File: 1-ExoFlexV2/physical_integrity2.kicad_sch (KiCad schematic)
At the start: 30 parts, among them J82 100k, J83 100k, J84 100k, J85 100k, J86 100k, J87 100k, U74 SN74LVC1G32DBVR, U75 SN74LVC1G32DBVR, U76 SN74LVC1G32DBVR, U77 SN74LVC1G32DBVR, U79 SN74LVC1G32DBVR

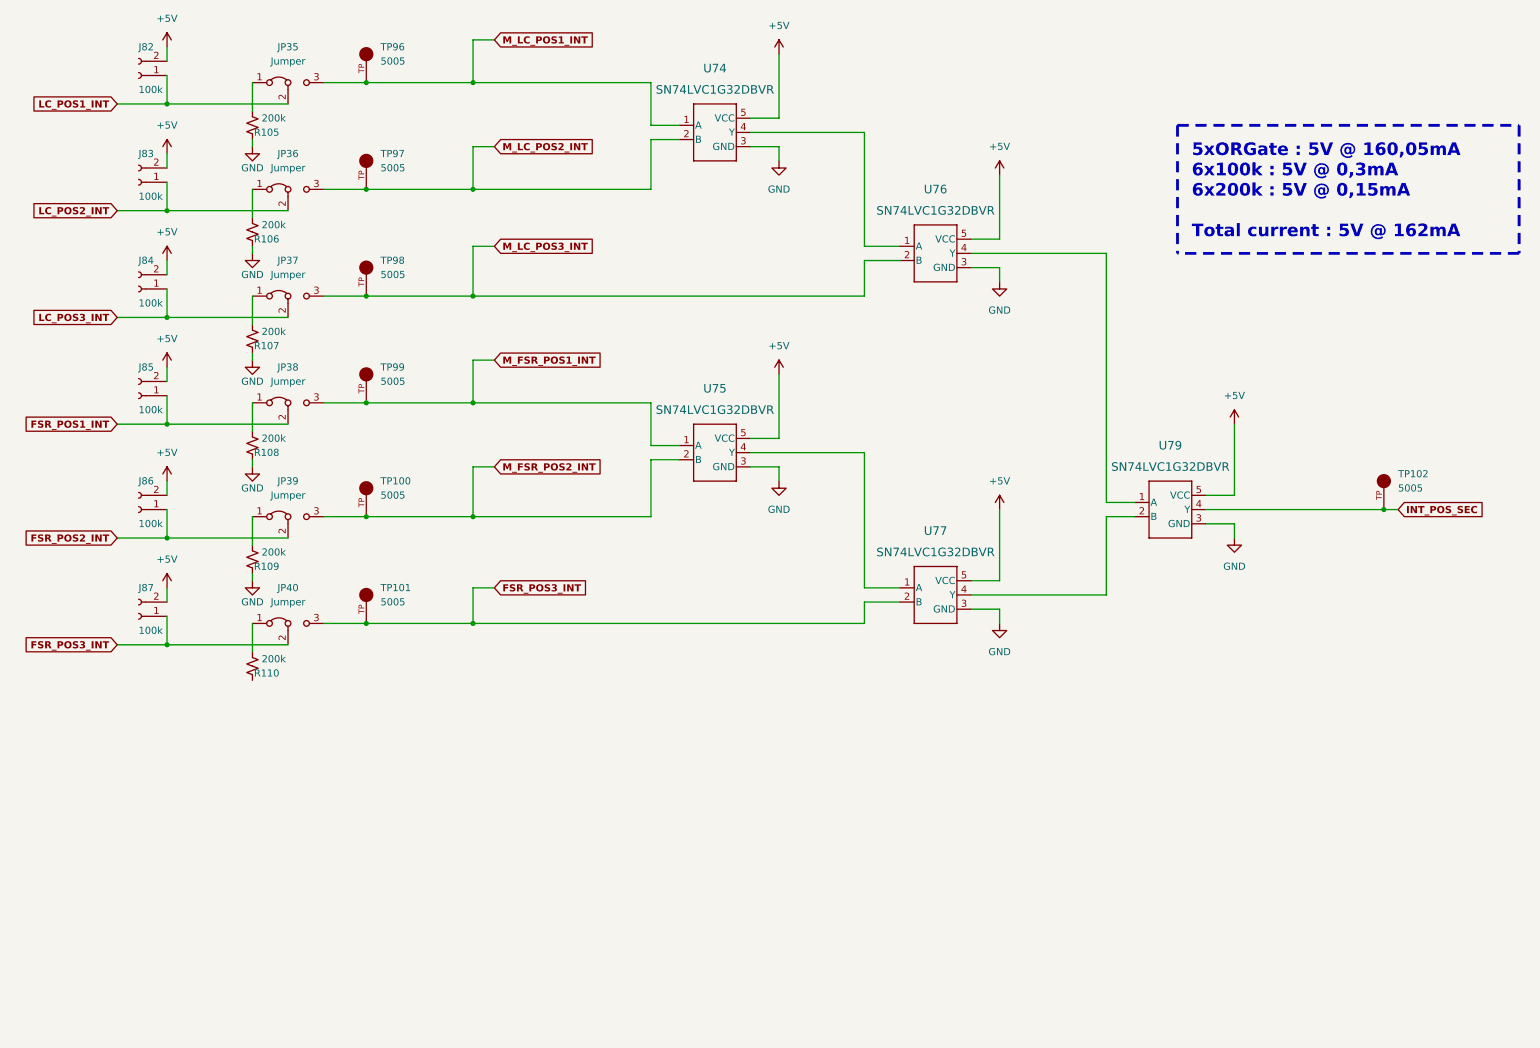
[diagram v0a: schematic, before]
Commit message: Chokes et RC
- Ajout des RF chokes
- Changement des résistance pour 0805
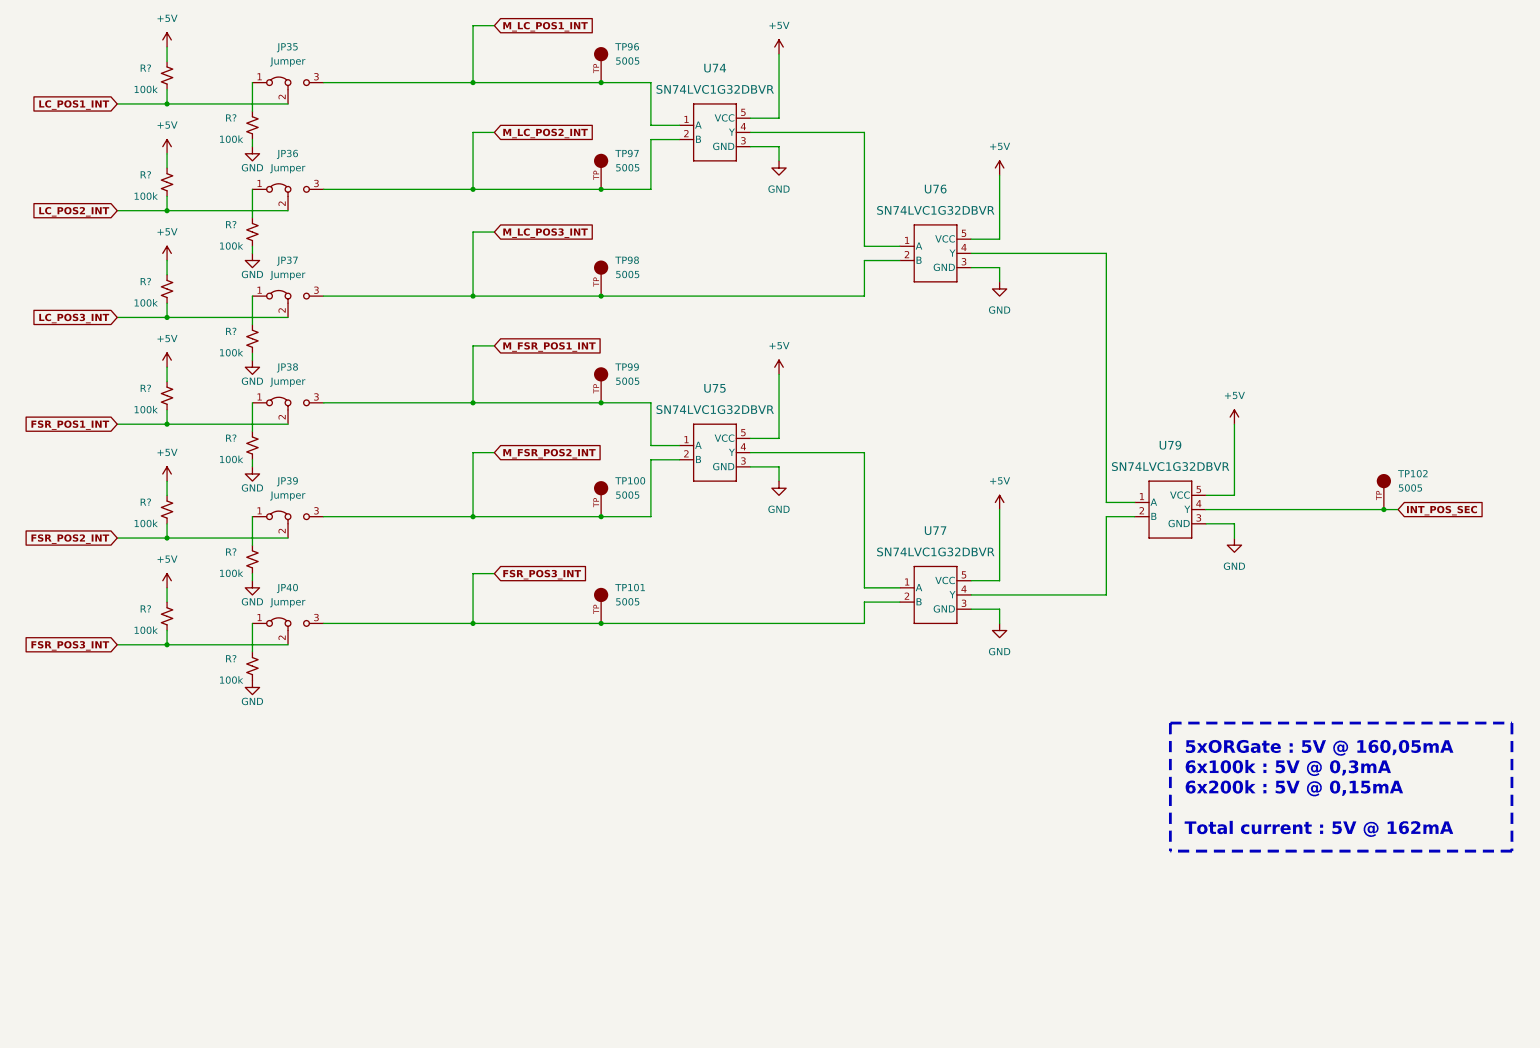
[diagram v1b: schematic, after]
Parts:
- removed J82, J83, J84, J85, J86, J87: 100k, Connector_PinHeader_2.54mm:PinHeader_1x02_P2.54mm_Vertical, symbol Connector:Conn_01x02_Female
- removed R105, R106, R107, R108, R109, R110: 200k, Resistor_SMD:R_0603_1608Metric, symbol Device:R_Small_US
- added R? (x12): 100k, Resistor_SMD:R_0805_2012Metric, symbol Device:R_Small_US
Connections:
- net +5V: now also R?.1, R?.1, R?.1, R?.1, R?.1, R?.1
- net FSR_POS1_INT: now also R?.2
- net FSR_POS2_INT: now also R?.2
- net FSR_POS3_INT: now also R?.2
- net GND: now also R?.2, R?.2, R?.2, R?.2, R?.2, R?.2
- net LC_POS1_INT: now also R?.2
- net LC_POS2_INT: now also R?.2
- net LC_POS3_INT: now also R?.2
- net at JP39.1 (A): now also R?.1
- net at JP38.1 (A): now also R?.1
- net at JP40.1 (A): now also R?.1
- net at JP37.1 (A): now also R?.1
- net at JP36.1 (A): now also R?.1
- net at JP35.1 (A): now also R?.1
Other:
- moved on the sheet: TP100, TP101, TP96, TP97, TP98, TP99

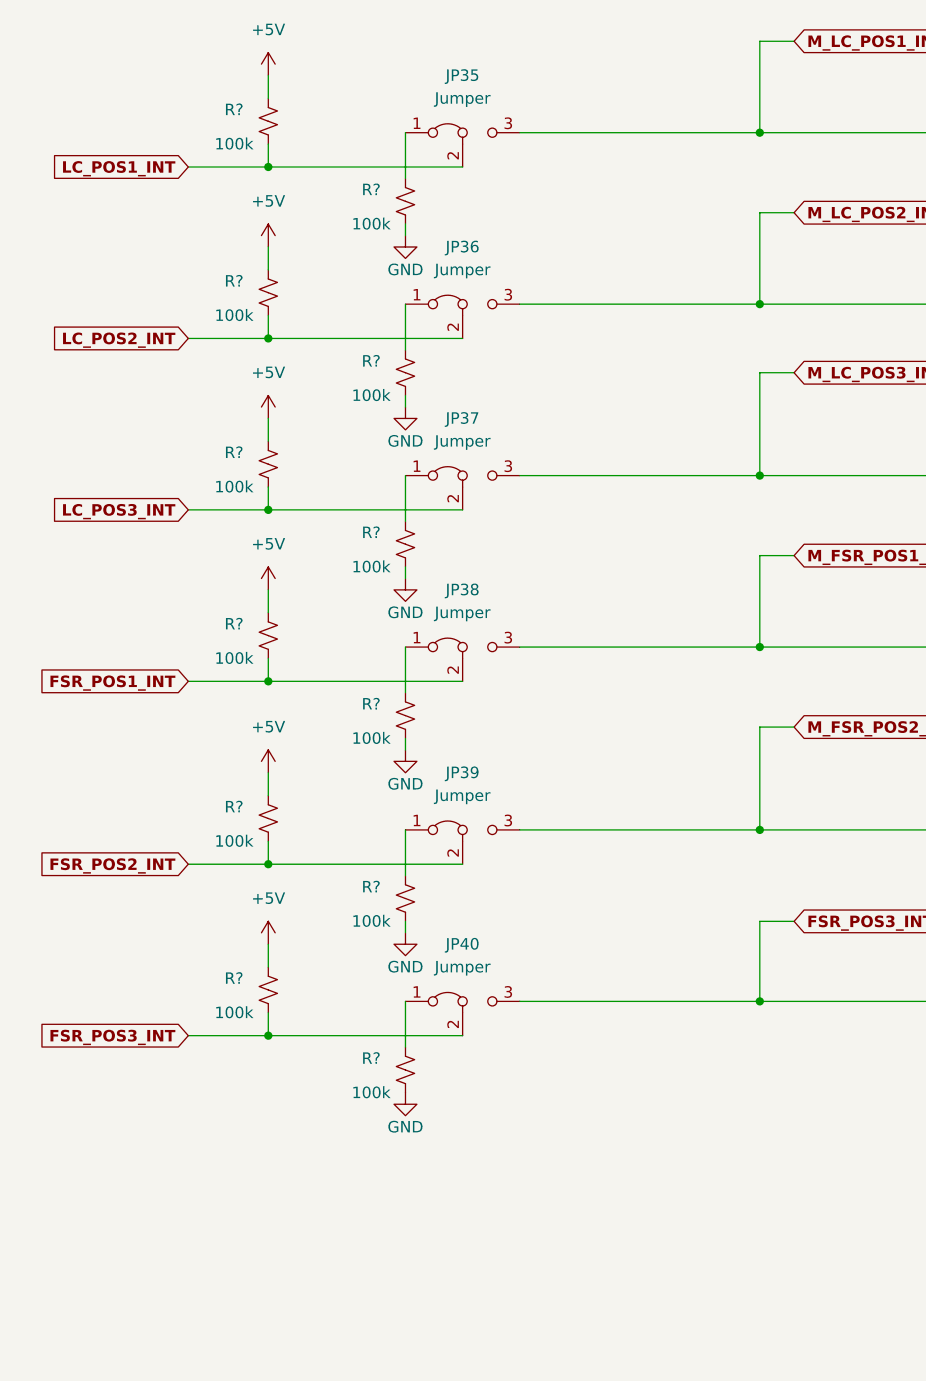
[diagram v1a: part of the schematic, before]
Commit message: Trimmer et jumper
-Changement de symbole de jumper
-Ajout des des trimmer aux endroits nécessaires
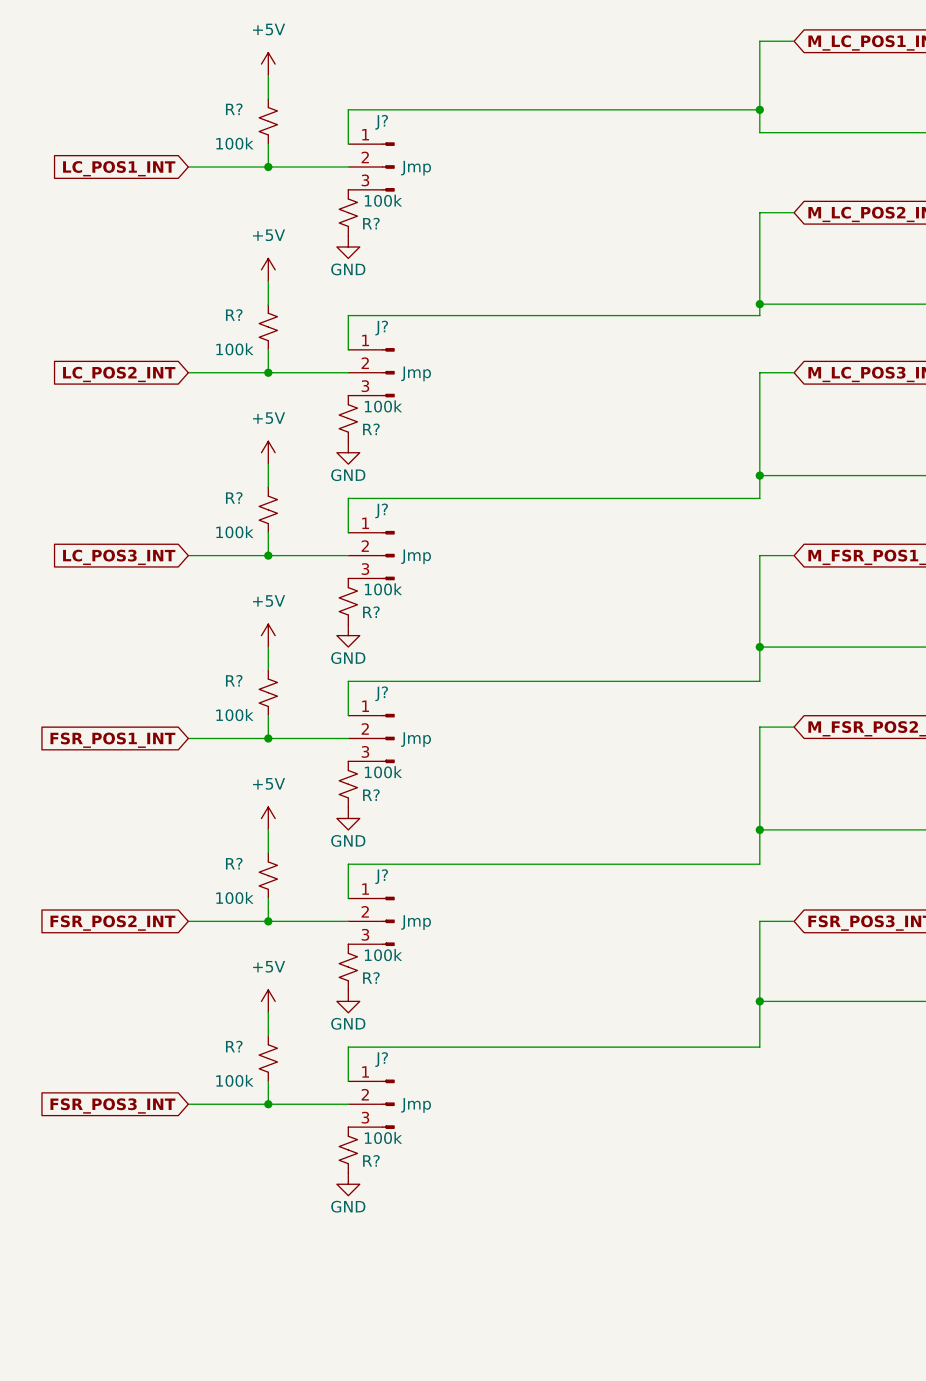
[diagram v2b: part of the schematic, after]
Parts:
- removed JP35, JP36, JP37, JP38, JP39, JP40: Jumper, Connector_PinHeader_2.54mm:PinHeader_1x03_P2.54mm_Vertical, symbol Jumper:Jumper_3_Bridged12
- removed R? (x6): 100k, Resistor_SMD:R_0805_2012Metric, symbol Device:R_Small_US
- added J? (x6): Jmp, symbol Connector:Conn_01x03_Male
- added R? (x6): 100k, Resistor_SMD:R_0805_2012Metric, symbol Device:R_Small_US
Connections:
- net FSR_POS1_INT: now also J?.2 (Pin_2)
- net FSR_POS2_INT: now also J?.2 (Pin_2)
- net FSR_POS3_INT: now also J?.1 (Pin_1), J?.2 (Pin_2)
- net GND: now also R?.2, R?.2, R?.2, R?.2, R?.2, R?.2
- net LC_POS1_INT: now also J?.2 (Pin_2)
- net LC_POS2_INT: now also J?.2 (Pin_2)
- net LC_POS3_INT: now also J?.2 (Pin_2)
- net M_FSR_POS1_INT: now also J?.1 (Pin_1)
- net M_FSR_POS2_INT: now also J?.1 (Pin_1)
- net M_LC_POS1_INT: now also J?.1 (Pin_1)
- net M_LC_POS2_INT: now also J?.1 (Pin_1)
- net M_LC_POS3_INT: now also J?.1 (Pin_1)
- new net: J?.3 (Pin_3), R?.1 (x6)
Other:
- moved on the sheet: R?

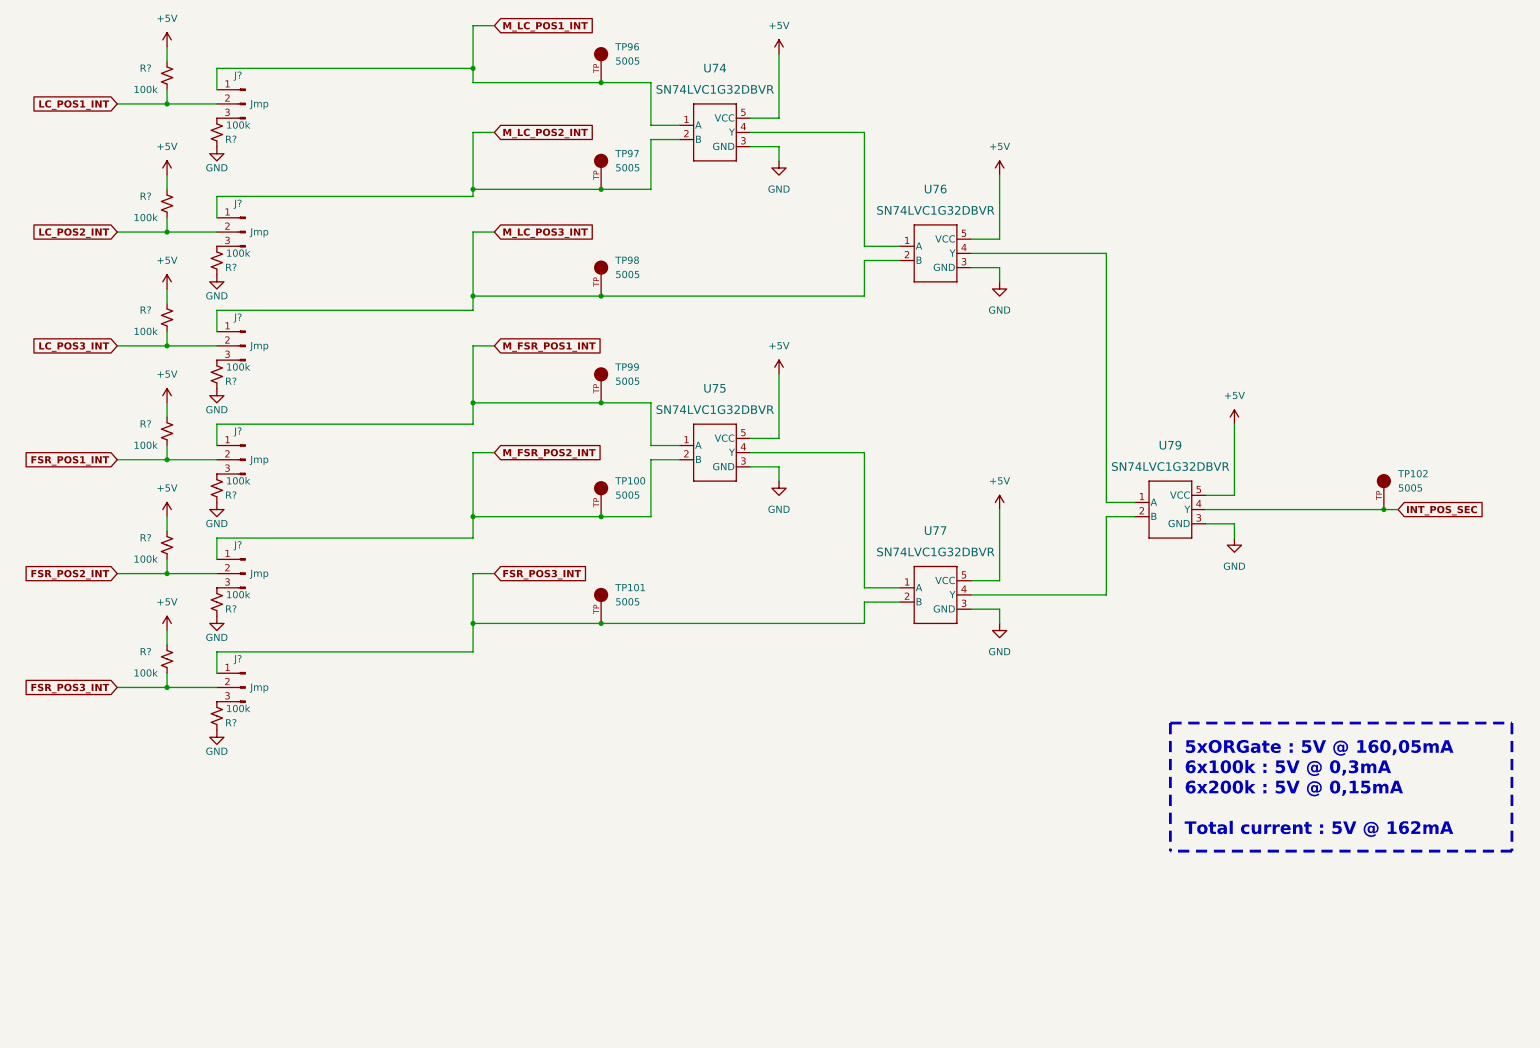
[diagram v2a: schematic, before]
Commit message: Test points et notes
- Ajout de tous les tests point nécessaires
-  Ajoute des sections de notes dans chaque page
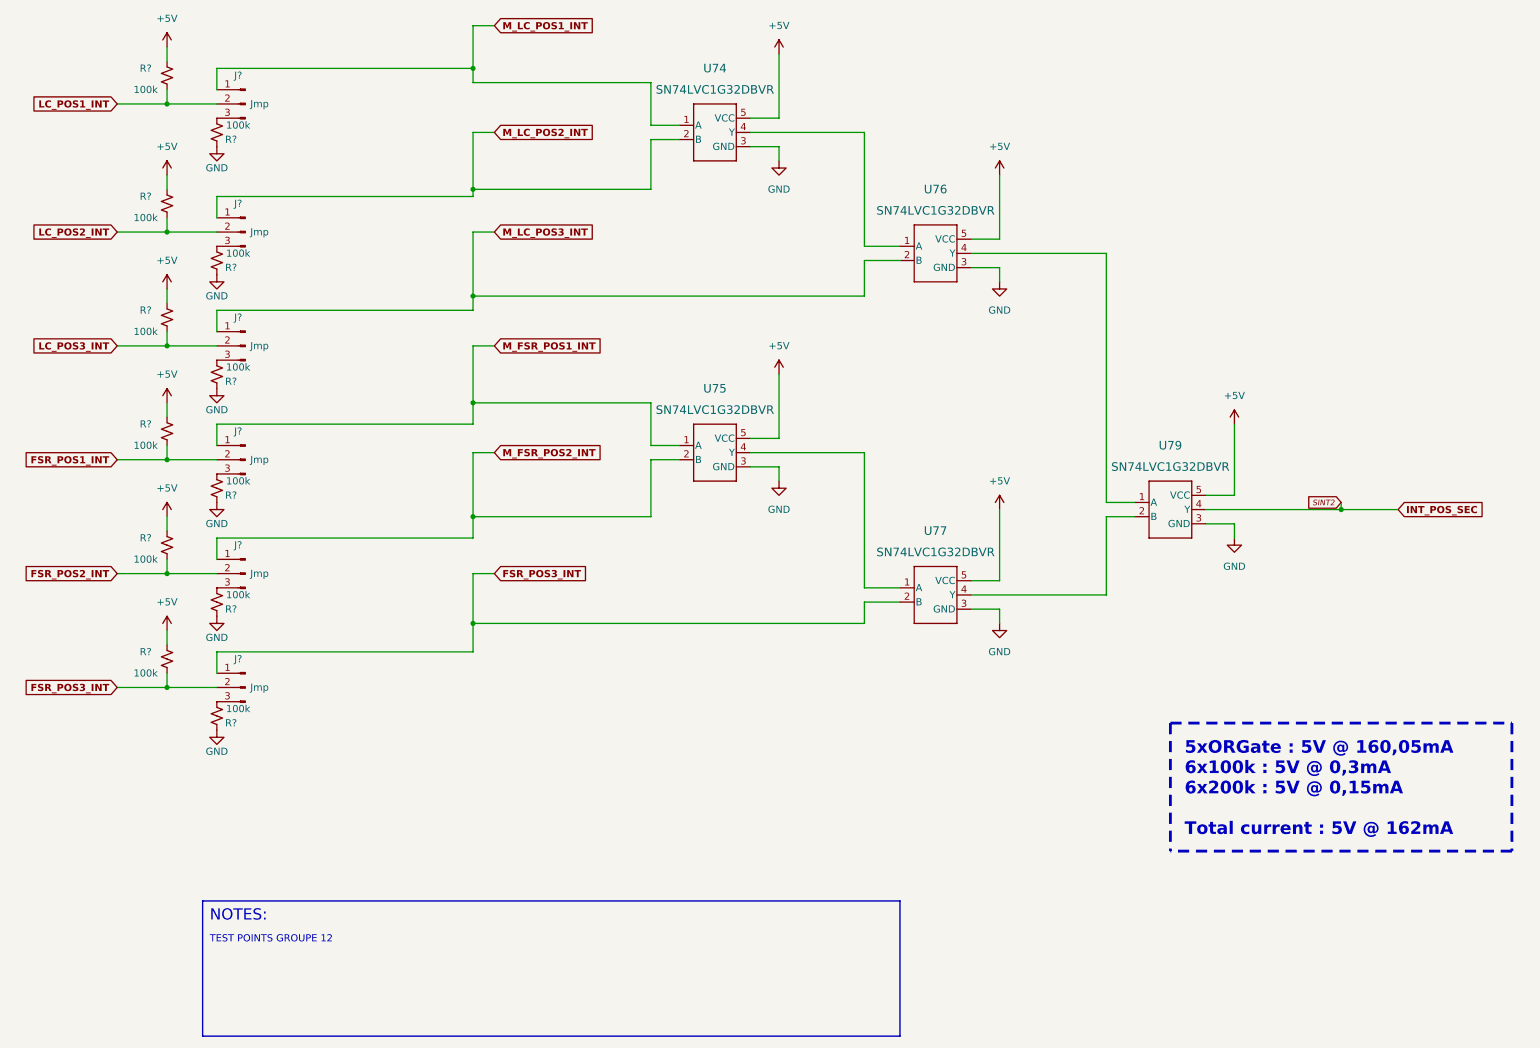
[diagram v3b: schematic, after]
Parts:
- removed TP100, TP101, TP102, TP96, TP97, TP98, TP99: 5005, FootPrint:KEYSTONE_5005, symbol SymLib:5005
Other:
- note added: "NOTES:"
- note added: "TEST POINTS GROUPE 12"
